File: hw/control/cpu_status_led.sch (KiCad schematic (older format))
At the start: 5 parts, among them Q401 BC817

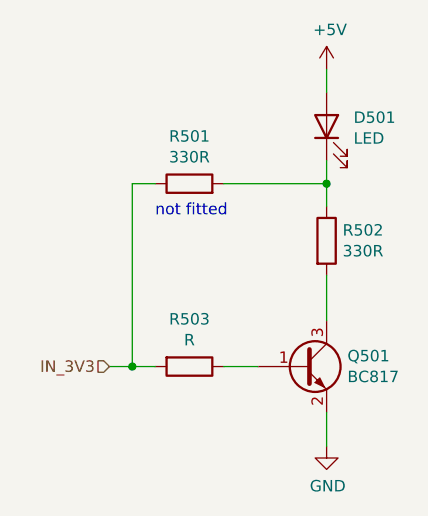
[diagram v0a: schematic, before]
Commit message: [hw] Add alternative LED data line from SPI
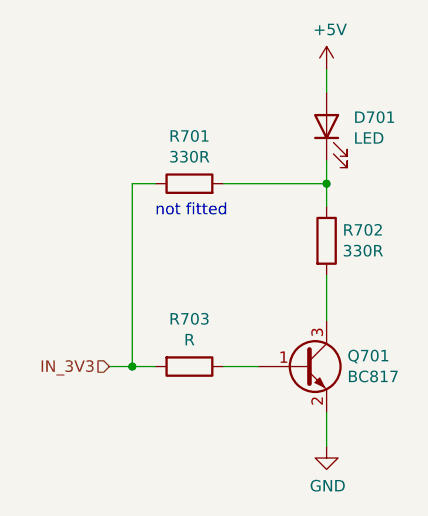
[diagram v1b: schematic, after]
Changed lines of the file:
@@
 AR Path="/6148E1AC/61836CD9/6182D735" Ref="R603"  Part="1"
 AR Path="/6148E1AC/61844B10/6182D735" Ref="R703"  Part="1"
-F 0 "R503" V 4693 4000 50  0000 C CNN
+F 0 "R703" V 4693 4000 50  0000 C CNN
 F 1 "R" V 4784 4000 50  0000 C CNN
 F 2 "" V 4830 4000 50  0001 C CNN
@@
 AR Path="/6148E1AC/61836CD9/6182D73B" Ref="Q601"  Part="1"
 AR Path="/6148E1AC/61844B10/6182D73B" Ref="Q701"  Part="1"
-F 0 "Q501" H 5591 4046 50  0000 L CNN
+F 0 "Q701" H 5591 4046 50  0000 L CNN
 F 1 "BC817" H 5591 3955 50  0000 L CNN
 F 2 "" H 5600 4100 50  0001 C CNN
@@
 AR Path="/6148E1AC/61836CD9/6182D99B" Ref="D601"  Part="1"
 AR Path="/6148E1AC/61844B10/6182D99B" Ref="D701"  Part="1"
-F 0 "D501" V 5539 2832 50  0000 R CNN
+F 0 "D701" V 5539 2832 50  0000 R CNN
 F 1 "LED" V 5448 2832 50  0000 R CNN
 F 2 "" H 5500 2950 50  0001 C CNN
@@
 AR Path="/6148E1AC/61836CD9/6182E435" Ref="R602"  Part="1"
 AR Path="/6148E1AC/61844B10/6182E435" Ref="R702"  Part="1"
-F 0 "R502" H 5570 3496 50  0000 L CNN
+F 0 "R702" H 5570 3496 50  0000 L CNN
 F 1 "330R" H 5570 3405 50  0000 L CNN
 F 2 "" V 5430 3450 50  0001 C CNN
@@
 AR Path="/6148E1AC/61836CD9/6189DFCF" Ref="R601"  Part="1"
 AR Path="/6148E1AC/61844B10/6189DFCF" Ref="R701"  Part="1"
-F 0 "R501" V 5107 3200 50  0000 C CNN
+F 0 "R701" V 5107 3200 50  0000 C CNN
 F 1 "330R" V 5016 3200 50  0000 C CNN
 F 2 "" V 4830 3200 50  0001 C CNN

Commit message: [hw] Assign most of the controller footprints
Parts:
- D401: footprint (none) -> LED_SMD:LED_0805_2012Metric_Pad1.15x1.40mm_HandSolder
- Q401: footprint (none) -> Package_TO_SOT_SMD:SOT-23_Handsoldering
- R401, R402, R403: footprint (none) -> Resistor_SMD:R_0805_2012Metric_Pad1.20x1.40mm_HandSolder
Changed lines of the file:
@@
 $Descr A4 11693 8268
 encoding utf-8
-Sheet 5 13
+Sheet 7 13
 Title "WS2812 Controller"
 Date "2021-10-10"
@@
 F 0 "R703" V 4693 4000 50  0000 C CNN
 F 1 "R" V 4784 4000 50  0000 C CNN
-F 2 "" V 4830 4000 50  0001 C CNN
+F 2 "Resistor_SMD:R_0805_2012Metric_Pad1.20x1.40mm_HandSolder" V 4830 4000 50  0001 C CNN
 F 3 "~" H 4900 4000 50  0001 C CNN
 	1    4900 4000
@@
 F 0 "Q701" H 5591 4046 50  0000 L CNN
 F 1 "BC817" H 5591 3955 50  0000 L CNN
-F 2 "" H 5600 4100 50  0001 C CNN
+F 2 "Package_TO_SOT_SMD:SOT-23_Handsoldering" H 5600 4100 50  0001 C CNN
 F 3 "~" H 5400 4000 50  0001 C CNN
 	1    5400 4000
@@
 F 0 "D701" V 5539 2832 50  0000 R CNN
 F 1 "LED" V 5448 2832 50  0000 R CNN
-F 2 "" H 5500 2950 50  0001 C CNN
+F 2 "LED_SMD:LED_0805_2012Metric_Pad1.15x1.40mm_HandSolder" H 5500 2950 50  0001 C CNN
 F 3 "~" H 5500 2950 50  0001 C CNN
 	1    5500 2950
@@
 F 0 "R702" H 5570 3496 50  0000 L CNN
 F 1 "330R" H 5570 3405 50  0000 L CNN
-F 2 "" V 5430 3450 50  0001 C CNN
+F 2 "Resistor_SMD:R_0805_2012Metric_Pad1.20x1.40mm_HandSolder" V 5430 3450 50  0001 C CNN
 F 3 "~" H 5500 3450 50  0001 C CNN
 	1    5500 3450
@@
 F 0 "R701" V 5107 3200 50  0000 C CNN
 F 1 "330R" V 5016 3200 50  0000 C CNN
-F 2 "" V 4830 3200 50  0001 C CNN
+F 2 "Resistor_SMD:R_0805_2012Metric_Pad1.20x1.40mm_HandSolder" V 4830 3200 50  0001 C CNN
 F 3 "~" H 4900 3200 50  0001 C CNN
 	1    4900 3200

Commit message: [hw] Incorporate suggestions
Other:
- note added: "Alternative\nNot mounted"
- note removed: "not fitted"
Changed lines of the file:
@@
 $Descr A4 11693 8268
 encoding utf-8
-Sheet 7 13
+Sheet 5 13
 Title "WS2812 Controller"
 Date "2021-10-10"
@@
 AR Path="/6148E1AC/61836CD9/6182751A" Ref="#PWR0601"  Part="1"
 AR Path="/6148E1AC/61844B10/6182751A" Ref="#PWR0701"  Part="1"
-F 0 "#PWR0701" H 5500 2550 50  0001 C CNN
+F 0 "#PWR0501" H 5500 2550 50  0001 C CNN
 F 1 "+5V" H 5515 2873 50  0000 C CNN
 F 2 "" H 5500 2700 50  0001 C CNN
@@
 AR Path="/6148E1AC/61836CD9/6182D735" Ref="R603"  Part="1"
 AR Path="/6148E1AC/61844B10/6182D735" Ref="R703"  Part="1"
-F 0 "R703" V 4693 4000 50  0000 C CNN
+F 0 "R503" V 4693 4000 50  0000 C CNN
 F 1 "R" V 4784 4000 50  0000 C CNN
 F 2 "Resistor_SMD:R_0805_2012Metric_Pad1.20x1.40mm_HandSolder" V 4830 4000 50  0001 C CNN
@@
 AR Path="/6148E1AC/61836CD9/6182D73B" Ref="Q601"  Part="1"
 AR Path="/6148E1AC/61844B10/6182D73B" Ref="Q701"  Part="1"
-F 0 "Q701" H 5591 4046 50  0000 L CNN
+F 0 "Q501" H 5591 4046 50  0000 L CNN
 F 1 "BC817" H 5591 3955 50  0000 L CNN
 F 2 "Package_TO_SOT_SMD:SOT-23_Handsoldering" H 5600 4100 50  0001 C CNN
@@
 AR Path="/6148E1AC/61836CD9/6182D99B" Ref="D601"  Part="1"
 AR Path="/6148E1AC/61844B10/6182D99B" Ref="D701"  Part="1"
-F 0 "D701" V 5539 2832 50  0000 R CNN
+F 0 "D501" V 5539 2832 50  0000 R CNN
 F 1 "LED" V 5448 2832 50  0000 R CNN
 F 2 "LED_SMD:LED_0805_2012Metric_Pad1.15x1.40mm_HandSolder" H 5500 2950 50  0001 C CNN
@@
 AR Path="/6148E1AC/61836CD9/6182E435" Ref="R602"  Part="1"
 AR Path="/6148E1AC/61844B10/6182E435" Ref="R702"  Part="1"
-F 0 "R702" H 5570 3496 50  0000 L CNN
+F 0 "R502" H 5570 3496 50  0000 L CNN
 F 1 "330R" H 5570 3405 50  0000 L CNN
 F 2 "Resistor_SMD:R_0805_2012Metric_Pad1.20x1.40mm_HandSolder" V 5430 3450 50  0001 C CNN
@@
 AR Path="/6148E1AC/61836CD9/6182FC68" Ref="#PWR0602"  Part="1"
 AR Path="/6148E1AC/61844B10/6182FC68" Ref="#PWR0702"  Part="1"
-F 0 "#PWR0702" H 5500 4100 50  0001 C CNN
+F 0 "#PWR0502" H 5500 4100 50  0001 C CNN
 F 1 "GND" H 5505 4177 50  0000 C CNN
 F 2 "" H 5500 4350 50  0001 C CNN
@@
 AR Path="/6148E1AC/61836CD9/6189DFCF" Ref="R601"  Part="1"
 AR Path="/6148E1AC/61844B10/6189DFCF" Ref="R701"  Part="1"
-F 0 "R701" V 5107 3200 50  0000 C CNN
+F 0 "R501" V 5107 3200 50  0000 C CNN
 F 1 "330R" V 5016 3200 50  0000 C CNN
 F 2 "Resistor_SMD:R_0805_2012Metric_Pad1.20x1.40mm_HandSolder" V 4830 3200 50  0001 C CNN
@@
 Wire Wire Line
 	4650 4000 4750 4000
-Text Notes 4750 3350 0    50   ~ 0
-not fitted
+Text Notes 4200 2950 0    50   ~ 0
+Alternative\nNot mounted
+Wire Notes Line
+	5150 3550 5150 2750
+Wire Notes Line
+	5150 2750 4150 2750
+Wire Notes Line
+	4150 2750 4150 3550
+Wire Notes Line
+	4150 3550 5150 3550
 $EndSCHEMATC

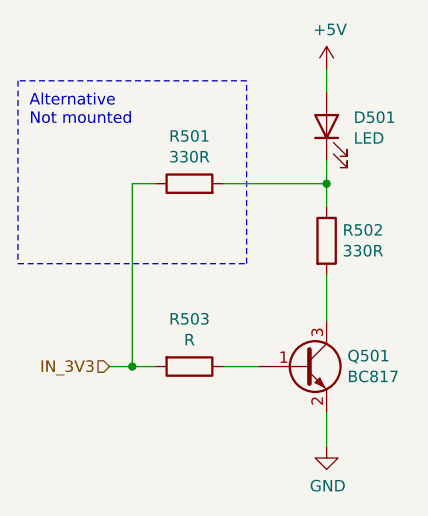
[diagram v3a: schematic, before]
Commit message: [hw] Assign control board footprints
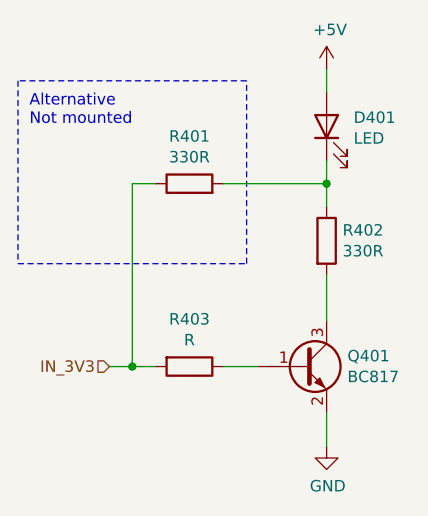
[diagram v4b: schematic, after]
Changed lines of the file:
@@
 $Descr A4 11693 8268
 encoding utf-8
-Sheet 5 13
+Sheet 4 13
 Title "WS2812 Controller"
 Date "2021-10-10"
@@
 AR Path="/6148E1AC/61836CD9/6182751A" Ref="#PWR0601"  Part="1"
 AR Path="/6148E1AC/61844B10/6182751A" Ref="#PWR0701"  Part="1"
-F 0 "#PWR0501" H 5500 2550 50  0001 C CNN
+F 0 "#PWR0701" H 5500 2550 50  0001 C CNN
 F 1 "+5V" H 5515 2873 50  0000 C CNN
 F 2 "" H 5500 2700 50  0001 C CNN
@@
 AR Path="/6148E1AC/61836CD9/6182D735" Ref="R603"  Part="1"
 AR Path="/6148E1AC/61844B10/6182D735" Ref="R703"  Part="1"
-F 0 "R503" V 4693 4000 50  0000 C CNN
+F 0 "R403" V 4693 4000 50  0000 C CNN
 F 1 "R" V 4784 4000 50  0000 C CNN
 F 2 "Resistor_SMD:R_0805_2012Metric_Pad1.20x1.40mm_HandSolder" V 4830 4000 50  0001 C CNN
@@
 AR Path="/6148E1AC/61836CD9/6182D73B" Ref="Q601"  Part="1"
 AR Path="/6148E1AC/61844B10/6182D73B" Ref="Q701"  Part="1"
-F 0 "Q501" H 5591 4046 50  0000 L CNN
+F 0 "Q401" H 5591 4046 50  0000 L CNN
 F 1 "BC817" H 5591 3955 50  0000 L CNN
 F 2 "Package_TO_SOT_SMD:SOT-23_Handsoldering" H 5600 4100 50  0001 C CNN
@@
 AR Path="/6148E1AC/61836CD9/6182D99B" Ref="D601"  Part="1"
 AR Path="/6148E1AC/61844B10/6182D99B" Ref="D701"  Part="1"
-F 0 "D501" V 5539 2832 50  0000 R CNN
+F 0 "D401" V 5539 2832 50  0000 R CNN
 F 1 "LED" V 5448 2832 50  0000 R CNN
 F 2 "LED_SMD:LED_0805_2012Metric_Pad1.15x1.40mm_HandSolder" H 5500 2950 50  0001 C CNN
@@
 AR Path="/6148E1AC/61836CD9/6182E435" Ref="R602"  Part="1"
 AR Path="/6148E1AC/61844B10/6182E435" Ref="R702"  Part="1"
-F 0 "R502" H 5570 3496 50  0000 L CNN
+F 0 "R402" H 5570 3496 50  0000 L CNN
 F 1 "330R" H 5570 3405 50  0000 L CNN
 F 2 "Resistor_SMD:R_0805_2012Metric_Pad1.20x1.40mm_HandSolder" V 5430 3450 50  0001 C CNN
@@
 AR Path="/6148E1AC/61836CD9/6182FC68" Ref="#PWR0602"  Part="1"
 AR Path="/6148E1AC/61844B10/6182FC68" Ref="#PWR0702"  Part="1"
-F 0 "#PWR0502" H 5500 4100 50  0001 C CNN
+F 0 "#PWR0702" H 5500 4100 50  0001 C CNN
 F 1 "GND" H 5505 4177 50  0000 C CNN
 F 2 "" H 5500 4350 50  0001 C CNN
@@
 AR Path="/6148E1AC/61836CD9/6189DFCF" Ref="R601"  Part="1"
 AR Path="/6148E1AC/61844B10/6189DFCF" Ref="R701"  Part="1"
-F 0 "R501" V 5107 3200 50  0000 C CNN
+F 0 "R401" V 5107 3200 50  0000 C CNN
 F 1 "330R" V 5016 3200 50  0000 C CNN
 F 2 "Resistor_SMD:R_0805_2012Metric_Pad1.20x1.40mm_HandSolder" V 4830 3200 50  0001 C CNN

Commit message: [hw] Update LED power supply
* Add 10 uF capacitors
* Add more space heat sinks
* Add thermal reliefs
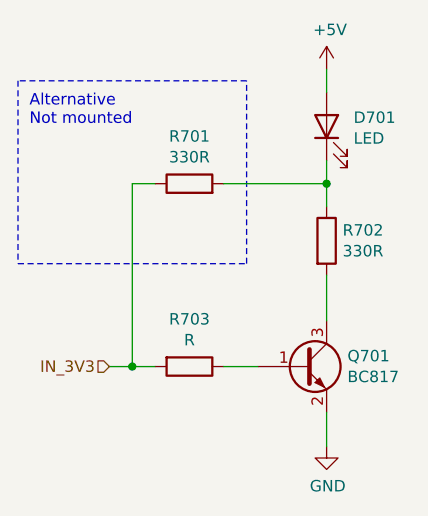
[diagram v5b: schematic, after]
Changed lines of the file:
@@
 AR Path="/6148E1AC/61836CD9/6182D735" Ref="R603"  Part="1"
 AR Path="/6148E1AC/61844B10/6182D735" Ref="R703"  Part="1"
-F 0 "R403" V 4693 4000 50  0000 C CNN
+F 0 "R703" V 4693 4000 50  0000 C CNN
 F 1 "R" V 4784 4000 50  0000 C CNN
 F 2 "Resistor_SMD:R_0805_2012Metric_Pad1.20x1.40mm_HandSolder" V 4830 4000 50  0001 C CNN
@@
 AR Path="/6148E1AC/61836CD9/6182D73B" Ref="Q601"  Part="1"
 AR Path="/6148E1AC/61844B10/6182D73B" Ref="Q701"  Part="1"
-F 0 "Q401" H 5591 4046 50  0000 L CNN
+F 0 "Q701" H 5591 4046 50  0000 L CNN
 F 1 "BC817" H 5591 3955 50  0000 L CNN
 F 2 "Package_TO_SOT_SMD:SOT-23_Handsoldering" H 5600 4100 50  0001 C CNN
@@
 AR Path="/6148E1AC/61836CD9/6182D99B" Ref="D601"  Part="1"
 AR Path="/6148E1AC/61844B10/6182D99B" Ref="D701"  Part="1"
-F 0 "D401" V 5539 2832 50  0000 R CNN
+F 0 "D701" V 5539 2832 50  0000 R CNN
 F 1 "LED" V 5448 2832 50  0000 R CNN
 F 2 "LED_SMD:LED_0805_2012Metric_Pad1.15x1.40mm_HandSolder" H 5500 2950 50  0001 C CNN
@@
 AR Path="/6148E1AC/61836CD9/6182E435" Ref="R602"  Part="1"
 AR Path="/6148E1AC/61844B10/6182E435" Ref="R702"  Part="1"
-F 0 "R402" H 5570 3496 50  0000 L CNN
+F 0 "R702" H 5570 3496 50  0000 L CNN
 F 1 "330R" H 5570 3405 50  0000 L CNN
 F 2 "Resistor_SMD:R_0805_2012Metric_Pad1.20x1.40mm_HandSolder" V 5430 3450 50  0001 C CNN
@@
 AR Path="/6148E1AC/61836CD9/6189DFCF" Ref="R601"  Part="1"
 AR Path="/6148E1AC/61844B10/6189DFCF" Ref="R701"  Part="1"
-F 0 "R401" V 5107 3200 50  0000 C CNN
+F 0 "R701" V 5107 3200 50  0000 C CNN
 F 1 "330R" V 5016 3200 50  0000 C CNN
 F 2 "Resistor_SMD:R_0805_2012Metric_Pad1.20x1.40mm_HandSolder" V 4830 3200 50  0001 C CNN

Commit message: [hw] Add 5V supply layout
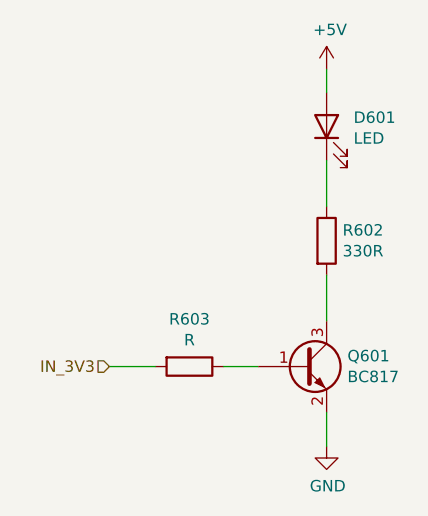
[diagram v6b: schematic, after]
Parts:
- removed R401: 330R, Resistor_SMD:R_0805_2012Metric_Pad1.20x1.40mm_HandSolder, symbol Device:R
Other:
- note removed: "Alternative\nNot mounted"
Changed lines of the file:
@@
 $Descr A4 11693 8268
 encoding utf-8
-Sheet 4 13
+Sheet 6 13
 Title "WS2812 Controller"
 Date "2021-10-10"
@@
 AR Path="/6148E1AC/61836CD9/6182751A" Ref="#PWR0601"  Part="1"
 AR Path="/6148E1AC/61844B10/6182751A" Ref="#PWR0701"  Part="1"
-F 0 "#PWR0701" H 5500 2550 50  0001 C CNN
+F 0 "#PWR0601" H 5500 2550 50  0001 C CNN
 F 1 "+5V" H 5515 2873 50  0000 C CNN
 F 2 "" H 5500 2700 50  0001 C CNN
@@
 AR Path="/6148E1AC/61836CD9/6182D735" Ref="R603"  Part="1"
 AR Path="/6148E1AC/61844B10/6182D735" Ref="R703"  Part="1"
-F 0 "R703" V 4693 4000 50  0000 C CNN
+F 0 "R603" V 4693 4000 50  0000 C CNN
 F 1 "R" V 4784 4000 50  0000 C CNN
 F 2 "Resistor_SMD:R_0805_2012Metric_Pad1.20x1.40mm_HandSolder" V 4830 4000 50  0001 C CNN
@@
 AR Path="/6148E1AC/61836CD9/6182D73B" Ref="Q601"  Part="1"
 AR Path="/6148E1AC/61844B10/6182D73B" Ref="Q701"  Part="1"
-F 0 "Q701" H 5591 4046 50  0000 L CNN
+F 0 "Q601" H 5591 4046 50  0000 L CNN
 F 1 "BC817" H 5591 3955 50  0000 L CNN
 F 2 "Package_TO_SOT_SMD:SOT-23_Handsoldering" H 5600 4100 50  0001 C CNN
@@
 Wire Wire Line
 	5500 3800 5500 3600
-Wire Wire Line
-	4550 4000 4650 4000
 $Comp
 L Device:LED D401
@@
 AR Path="/6148E1AC/61836CD9/6182D99B" Ref="D601"  Part="1"
 AR Path="/6148E1AC/61844B10/6182D99B" Ref="D701"  Part="1"
-F 0 "D701" V 5539 2832 50  0000 R CNN
+F 0 "D601" V 5539 2832 50  0000 R CNN
 F 1 "LED" V 5448 2832 50  0000 R CNN
 F 2 "LED_SMD:LED_0805_2012Metric_Pad1.15x1.40mm_HandSolder" H 5500 2950 50  0001 C CNN
@@
 AR Path="/6148E1AC/61836CD9/6182E435" Ref="R602"  Part="1"
 AR Path="/6148E1AC/61844B10/6182E435" Ref="R702"  Part="1"
-F 0 "R702" H 5570 3496 50  0000 L CNN
+F 0 "R602" H 5570 3496 50  0000 L CNN
 F 1 "330R" H 5570 3405 50  0000 L CNN
 F 2 "Resistor_SMD:R_0805_2012Metric_Pad1.20x1.40mm_HandSolder" V 5430 3450 50  0001 C CNN
@@
 AR Path="/6148E1AC/61836CD9/6182FC68" Ref="#PWR0602"  Part="1"
 AR Path="/6148E1AC/61844B10/6182FC68" Ref="#PWR0702"  Part="1"
-F 0 "#PWR0702" H 5500 4100 50  0001 C CNN
+F 0 "#PWR0602" H 5500 4100 50  0001 C CNN
 F 1 "GND" H 5505 4177 50  0000 C CNN
 F 2 "" H 5500 4350 50  0001 C CNN
@@
 	5500 4200 5500 4350
 Wire Wire Line
-	5500 3100 5500 3200
+	5500 2700 5500 2800
 Wire Wire Line
-	5500 2700 5500 2800
-$Comp
-L Device:R R401
-U 1 1 6189DFCF
-P 4900 3200
-AR Path="/6148E1AC/6182662F/6189DFCF" Ref="R401"  Part="1"
-AR Path="/6148E1AC/61831583/6189DFCF" Ref="R501"  Part="1"
-AR Path="/6148E1AC/61836CD9/6189DFCF" Ref="R601"  Part="1"
-AR Path="/6148E1AC/61844B10/6189DFCF" Ref="R701"  Part="1"
-F 0 "R701" V 5107 3200 50  0000 C CNN
-F 1 "330R" V 5016 3200 50  0000 C CNN
-F 2 "Resistor_SMD:R_0805_2012Metric_Pad1.20x1.40mm_HandSolder" V 4830 3200 50  0001 C CNN
-F 3 "~" H 4900 3200 50  0001 C CNN
-	1    4900 3200
-	0    -1   -1   0
-$EndComp
+	5500 3100 5500 3300
 Wire Wire Line
-	5050 3200 5500 3200
-Connection ~ 5500 3200
-Wire Wire Line
-	5500 3200 5500 3300
-Wire Wire Line
-	4750 3200 4650 3200
-Wire Wire Line
-	4650 3200 4650 4000
-Connection ~ 4650 4000
-Wire Wire Line
-	4650 4000 4750 4000
-Text Notes 4200 2950 0    50   ~ 0
-Alternative\nNot mounted
-Wire Notes Line
-	5150 3550 5150 2750
-Wire Notes Line
-	5150 2750 4150 2750
-Wire Notes Line
-	4150 2750 4150 3550
-Wire Notes Line
-	4150 3550 5150 3550
+	4550 4000 4750 4000
 $EndSCHEMATC

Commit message: [hw] Add layout of multiple subsystems
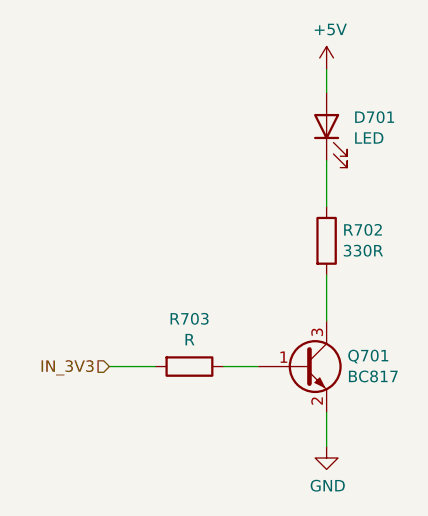
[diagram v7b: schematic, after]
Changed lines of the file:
@@
 $Descr A4 11693 8268
 encoding utf-8
-Sheet 6 13
+Sheet 7 13
 Title "WS2812 Controller"
 Date "2021-10-10"
@@
 AR Path="/6148E1AC/61836CD9/6182751A" Ref="#PWR0601"  Part="1"
 AR Path="/6148E1AC/61844B10/6182751A" Ref="#PWR0701"  Part="1"
-F 0 "#PWR0601" H 5500 2550 50  0001 C CNN
+F 0 "#PWR0701" H 5500 2550 50  0001 C CNN
 F 1 "+5V" H 5515 2873 50  0000 C CNN
 F 2 "" H 5500 2700 50  0001 C CNN
@@
 AR Path="/6148E1AC/61836CD9/6182D735" Ref="R603"  Part="1"
 AR Path="/6148E1AC/61844B10/6182D735" Ref="R703"  Part="1"
-F 0 "R603" V 4693 4000 50  0000 C CNN
+F 0 "R703" V 4693 4000 50  0000 C CNN
 F 1 "R" V 4784 4000 50  0000 C CNN
 F 2 "Resistor_SMD:R_0805_2012Metric_Pad1.20x1.40mm_HandSolder" V 4830 4000 50  0001 C CNN
@@
 AR Path="/6148E1AC/61836CD9/6182D73B" Ref="Q601"  Part="1"
 AR Path="/6148E1AC/61844B10/6182D73B" Ref="Q701"  Part="1"
-F 0 "Q601" H 5591 4046 50  0000 L CNN
+F 0 "Q701" H 5591 4046 50  0000 L CNN
 F 1 "BC817" H 5591 3955 50  0000 L CNN
 F 2 "Package_TO_SOT_SMD:SOT-23_Handsoldering" H 5600 4100 50  0001 C CNN
@@
 AR Path="/6148E1AC/61836CD9/6182D99B" Ref="D601"  Part="1"
 AR Path="/6148E1AC/61844B10/6182D99B" Ref="D701"  Part="1"
-F 0 "D601" V 5539 2832 50  0000 R CNN
+F 0 "D701" V 5539 2832 50  0000 R CNN
 F 1 "LED" V 5448 2832 50  0000 R CNN
 F 2 "LED_SMD:LED_0805_2012Metric_Pad1.15x1.40mm_HandSolder" H 5500 2950 50  0001 C CNN
@@
 AR Path="/6148E1AC/61836CD9/6182E435" Ref="R602"  Part="1"
 AR Path="/6148E1AC/61844B10/6182E435" Ref="R702"  Part="1"
-F 0 "R602" H 5570 3496 50  0000 L CNN
+F 0 "R702" H 5570 3496 50  0000 L CNN
 F 1 "330R" H 5570 3405 50  0000 L CNN
 F 2 "Resistor_SMD:R_0805_2012Metric_Pad1.20x1.40mm_HandSolder" V 5430 3450 50  0001 C CNN
@@
 AR Path="/6148E1AC/61836CD9/6182FC68" Ref="#PWR0602"  Part="1"
 AR Path="/6148E1AC/61844B10/6182FC68" Ref="#PWR0702"  Part="1"
-F 0 "#PWR0602" H 5500 4100 50  0001 C CNN
+F 0 "#PWR0702" H 5500 4100 50  0001 C CNN
 F 1 "GND" H 5505 4177 50  0000 C CNN
 F 2 "" H 5500 4350 50  0001 C CNN

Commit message: [hw] Improve control layout
Compacted 5V power supply, laid-out SD card holder to the RPi.
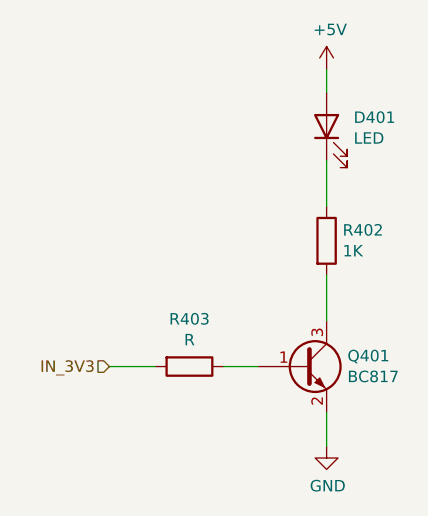
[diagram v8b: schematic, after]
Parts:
- R402: value 330R -> 1K
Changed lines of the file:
@@
 $Descr A4 11693 8268
 encoding utf-8
-Sheet 7 13
+Sheet 4 13
 Title "WS2812 Controller"
 Date "2021-10-10"
@@
 AR Path="/6148E1AC/61836CD9/6182751A" Ref="#PWR0601"  Part="1"
 AR Path="/6148E1AC/61844B10/6182751A" Ref="#PWR0701"  Part="1"
-F 0 "#PWR0701" H 5500 2550 50  0001 C CNN
+F 0 "#PWR0401" H 5500 2550 50  0001 C CNN
 F 1 "+5V" H 5515 2873 50  0000 C CNN
 F 2 "" H 5500 2700 50  0001 C CNN
@@
 AR Path="/6148E1AC/61836CD9/6182D735" Ref="R603"  Part="1"
 AR Path="/6148E1AC/61844B10/6182D735" Ref="R703"  Part="1"
-F 0 "R703" V 4693 4000 50  0000 C CNN
+F 0 "R403" V 4693 4000 50  0000 C CNN
 F 1 "R" V 4784 4000 50  0000 C CNN
 F 2 "Resistor_SMD:R_0805_2012Metric_Pad1.20x1.40mm_HandSolder" V 4830 4000 50  0001 C CNN
@@
 AR Path="/6148E1AC/61836CD9/6182D73B" Ref="Q601"  Part="1"
 AR Path="/6148E1AC/61844B10/6182D73B" Ref="Q701"  Part="1"
-F 0 "Q701" H 5591 4046 50  0000 L CNN
+F 0 "Q401" H 5591 4046 50  0000 L CNN
 F 1 "BC817" H 5591 3955 50  0000 L CNN
 F 2 "Package_TO_SOT_SMD:SOT-23_Handsoldering" H 5600 4100 50  0001 C CNN
@@
 AR Path="/6148E1AC/61836CD9/6182D99B" Ref="D601"  Part="1"
 AR Path="/6148E1AC/61844B10/6182D99B" Ref="D701"  Part="1"
-F 0 "D701" V 5539 2832 50  0000 R CNN
+F 0 "D401" V 5539 2832 50  0000 R CNN
 F 1 "LED" V 5448 2832 50  0000 R CNN
 F 2 "LED_SMD:LED_0805_2012Metric_Pad1.15x1.40mm_HandSolder" H 5500 2950 50  0001 C CNN
@@
 AR Path="/6148E1AC/61836CD9/6182E435" Ref="R602"  Part="1"
 AR Path="/6148E1AC/61844B10/6182E435" Ref="R702"  Part="1"
-F 0 "R702" H 5570 3496 50  0000 L CNN
-F 1 "330R" H 5570 3405 50  0000 L CNN
+F 0 "R402" H 5570 3496 50  0000 L CNN
+F 1 "1K" H 5570 3405 50  0000 L CNN
 F 2 "Resistor_SMD:R_0805_2012Metric_Pad1.20x1.40mm_HandSolder" V 5430 3450 50  0001 C CNN
 F 3 "~" H 5500 3450 50  0001 C CNN
@@
 AR Path="/6148E1AC/61836CD9/6182FC68" Ref="#PWR0602"  Part="1"
 AR Path="/6148E1AC/61844B10/6182FC68" Ref="#PWR0702"  Part="1"
-F 0 "#PWR0702" H 5500 4100 50  0001 C CNN
+F 0 "#PWR0402" H 5500 4100 50  0001 C CNN
 F 1 "GND" H 5505 4177 50  0000 C CNN
 F 2 "" H 5500 4350 50  0001 C CNN
